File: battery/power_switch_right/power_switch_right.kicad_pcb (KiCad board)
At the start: 2 copper layers, 1 part

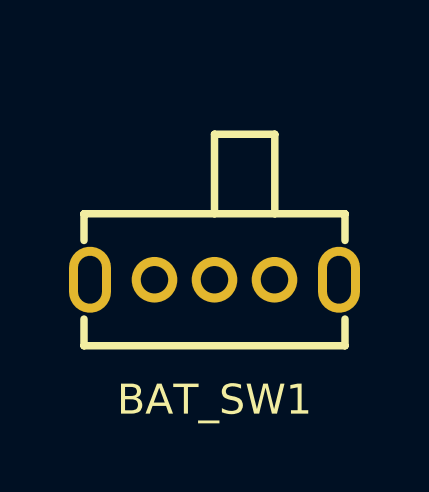
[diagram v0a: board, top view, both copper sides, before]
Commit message: use SK12D07VG5
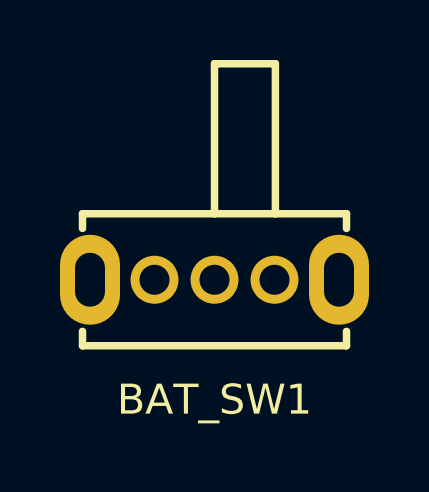
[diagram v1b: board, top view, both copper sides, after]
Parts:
- BAT_SW1: value ~ -> SK12D07VG5; footprint ErgoCai.pretty:SW-TH_SK12D07VG4 -> ErgoCai.pretty:SW-TH_SK12D07VG5-1
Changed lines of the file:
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@@
 	(net 3 "GND")
 	(net 4 "unconnected-(BAT_SW1-Pad3)")
-	(footprint "ErgoCai.pretty:SW-TH_SK12D07VG4"
+	(footprint "ErgoCai.pretty:SW-TH_SK12D07VG5-1"
 		(layer "F.Cu")
 		(at 0 0 180)
 		(property "Reference" "BAT_SW1"
-			(at 0 -4 180)
-			(layer "F.SilkS")
-			(effects
-				(font
-					(size 1 1)
-					(thickness 0.15)
-				)
-			)
-		)
-		(property "Value" "~"
-			(at 0 4 180)
-			(layer "F.Fab")
-			(effects
-				(font
-					(size 1 1)
-					(thickness 0.15)
-				)
-			)
-		)
-		(property "Datasheet" "https://lcsc.com/product-detail/Toggle-Switches_SHOU-HAN-SK12D07VG4_C393937.html"
-			(at 0 0 180)
+			(at 0 -4 0)
+			(layer "F.SilkS")
+			(effects
+				(font
+					(size 1 1)
+					(thickness 0.15)
+				)
+			)
+		)
+		(property "Value" "SK12D07VG5"
+			(at 0 4 0)
+			(layer "F.Fab")
+			(effects
+				(font
+					(size 1 1)
+					(thickness 0.15)
+				)
+			)
+		)
+		(property "Datasheet" "https://lcsc.com/product-detail/Toggle-Switches_SHOU-HAN-SK12D07VG5_C431548.html"
+			(at 0 0 0)
 			(layer "F.Fab")
 			(hide yes)
@@
 			)
 		)
-		(property "Description" "Switch, dual pole double throw, separate symbols"
-			(at 0 0 180)
+		(property "Description" ""
+			(at 0 0 0)
 			(layer "F.Fab")
 			(hide yes)
@@
 			)
 		)
-		(property "MF" "C&K"
-			(at 0 0 180)
-			(unlocked yes)
-			(layer "F.Fab")
-			(hide yes)
-			(effects
-				(font
-					(size 1 1)
-					(thickness 0.15)
-				)
-			)
-		)
-		(property "Description_1" "Switch Slide ON ON SPDT Side Slide 0.3A 30VDC PC Pins Bracket Mount/Through Hole Bulk"
-			(at 0 0 180)
-			(unlocked yes)
-			(layer "F.Fab")
-			(hide yes)
-			(effects
-				(font
-					(size 1 1)
-					(thickness 0.15)
-				)
-			)
-		)
-		(property "Package" "None"
-			(at 0 0 180)
-			(unlocked yes)
-			(layer "F.Fab")
-			(hide yes)
-			(effects
-				(font
-					(size 1 1)
-					(thickness 0.15)
-				)
-			)
-		)
-		(property "Price" "None"
-			(at 0 0 180)
-			(unlocked yes)
-			(layer "F.Fab")
-			(hide yes)
-			(effects
-				(font
-					(size 1 1)
-					(thickness 0.15)
-				)
-			)
-		)
-		(property "SnapEDA_Link" "https://www.snapeda.com/parts/SK12D07VG4/C%2526K/view-part/?ref=snap"
-			(at 0 0 180)
-			(unlocked yes)
-			(layer "F.Fab")
-			(hide yes)
-			(effects
-				(font
-					(size 1 1)
-					(thickness 0.15)
-				)
-			)
-		)
-		(property "MP" "SK12D07VG4"
-			(at 0 0 180)
-			(unlocked yes)
-			(layer "F.Fab")
-			(hide yes)
-			(effects
-				(font
-					(size 1 1)
-					(thickness 0.15)
-				)
-			)
-		)
-		(property "Availability" "Not in stock"
-			(at 0 0 180)
-			(unlocked yes)
-			(layer "F.Fab")
-			(hide yes)
-			(effects
-				(font
-					(size 1 1)
-					(thickness 0.15)
-				)
-			)
-		)
-		(property "Check_prices" "https://www.snapeda.com/parts/SK12D07VG4/C%2526K/view-part/?ref=eda"
-			(at 0 0 180)
-			(unlocked yes)
-			(layer "F.Fab")
-			(hide yes)
-			(effects
-				(font
-					(size 1 1)
-					(thickness 0.15)
-				)
-			)
-		)
-		(property "LCSC Part" "C393937"
+		(property "LCSC Part" "C431548"
 			(at 0 0 180)
 			(unlocked yes)
@@
 		(attr through_hole)
 		(fp_line
-			(start 4.35 2.2)
-			(end -4.35 2.2)
-			(stroke
-				(width 0.25)
-				(type solid)
-			)
-			(layer "F.SilkS")
-		)
-		(fp_line
-			(start 4.35 1.31)
-			(end 4.35 2.2)
-			(stroke
-				(width 0.25)
-				(type solid)
-			)
-			(layer "F.SilkS")
-		)
-		(fp_line
-			(start 4.35 -2.2)
-			(end 4.35 -1.31)
-			(stroke
-				(width 0.25)
-				(type solid)
-			)
-			(layer "F.SilkS")
-		)
-		(fp_line
-			(start 0 4.85)
-			(end 0 2.2)
-			(stroke
-				(width 0.25)
-				(type solid)
-			)
-			(layer "F.SilkS")
-		)
-		(fp_line
-			(start -2.01 4.85)
-			(end 0 4.85)
-			(stroke
-				(width 0.25)
-				(type solid)
-			)
-			(layer "F.SilkS")
-		)
-		(fp_line
-			(start -2.01 2.2)
-			(end -2.01 4.85)
-			(stroke
-				(width 0.25)
-				(type solid)
-			)
-			(layer "F.SilkS")
-		)
-		(fp_line
-			(start -4.35 2.2)
-			(end -4.35 1.31)
-			(stroke
-				(width 0.25)
-				(type solid)
-			)
-			(layer "F.SilkS")
-		)
-		(fp_line
-			(start -4.35 -1.31)
-			(end -4.35 -2.2)
-			(stroke
-				(width 0.25)
-				(type solid)
-			)
-			(layer "F.SilkS")
-		)
-		(fp_line
-			(start -4.35 -2.2)
-			(end 4.35 -2.2)
+			(start 4.4 2.2)
+			(end -4.4 2.2)
+			(stroke
+				(width 0.25)
+				(type solid)
+			)
+			(layer "F.SilkS")
+		)
+		(fp_line
+			(start 4.4 1.71)
+			(end 4.4 2.2)
+			(stroke
+				(width 0.25)
+				(type solid)
+			)
+			(layer "F.SilkS")
+		)
+		(fp_line
+			(start 4.4 -2.2)
+			(end 4.4 -1.72)
+			(stroke
+				(width 0.25)
+				(type solid)
+			)
+			(layer "F.SilkS")
+		)
+		(fp_line
+			(start 4.4 -2.2)
+			(end -4.4 -2.2)
+			(stroke
+				(width 0.25)
+				(type solid)
+			)
+			(layer "F.SilkS")
+		)
+		(fp_line
+			(start 0 2.2)
+			(end 0 7.2)
+			(stroke
+				(width 0.25)
+				(type solid)
+			)
+			(layer "F.SilkS")
+		)
+		(fp_line
+			(start -2.03 7.2)
+			(end 0 7.2)
+			(stroke
+				(width 0.25)
+				(type solid)
+			)
+			(layer "F.SilkS")
+		)
+		(fp_line
+			(start -2.03 7.2)
+			(end -2.03 2.2)
+			(stroke
+				(width 0.25)
+				(type solid)
+			)
+			(layer "F.SilkS")
+		)
+		(fp_line
+			(start -4.4 1.71)
+			(end -4.4 2.2)
+			(stroke
+				(width 0.25)
+				(type solid)
+			)
+			(layer "F.SilkS")
+		)
+		(fp_line
+			(start -4.4 -2.2)
+			(end -4.4 -1.72)
 			(stroke
 				(width 0.25)
@@
 		)
 		(fp_rect
-			(start -4.9 -2.4)
-			(end 4.9 2.4)
+			(start -5.5 -2.5)
+			(end 5.5 2.5)
 			(stroke
 				(width 0.05)
-				(type solid)
+				(type default)
 			)
 			(fill no)
 			(layer "F.CrtYd")
 		)
-		(fp_circle
-			(center -4.47 2.2)
-			(end -4.44 2.2)
-			(stroke
-				(width 0.06)
-				(type solid)
-			)
-			(fill no)
-			(layer "F.Fab")
-		)
 		(fp_text user "${REFERENCE}"
-			(at 0 0 180)
-			(layer "F.Fab")
-			(effects
-				(font
-					(size 1 1)
-					(thickness 0.15)
-				)
-			)
-		)
-		(pad "1" thru_hole circle
-			(at -2 0 180)
-			(size 1.52 1.52)
-			(drill 0.9144)
+			(at 0 0 0)
+			(layer "F.Fab")
+			(effects
+				(font
+					(size 1 1)
+					(thickness 0.15)
+				)
+			)
+		)
+		(pad "1" thru_hole oval
+			(at -2 0)
+			(size 1.6 1.6)
+			(drill 0.999998)
 			(layers "*.Cu" "*.Mask")
 			(remove_unused_layers no)
@@
 			(pintype "unspecified")
 		)
-		(pad "2" thru_hole circle
-			(at 0 0 180)
-			(size 1.52 1.52)
-			(drill 0.9144)
+		(pad "2" thru_hole oval
+			(at 0 0)
+			(size 1.6 1.6)
+			(drill 0.999998)
 			(layers "*.Cu" "*.Mask")
 			(remove_unused_layers no)
@@
 			(pintype "unspecified")
 		)
-		(pad "3" thru_hole circle
-			(at 2 0 180)
-			(size 1.52 1.52)
-			(drill 0.9144)
+		(pad "3" thru_hole oval
+			(at 2 0)
+			(size 1.6 1.6)
+			(drill 0.999998)
 			(layers "*.Cu" "*.Mask")
 			(remove_unused_layers no)
@@
 		)
 		(pad "4" thru_hole oval
-			(at 4.15 0 180)
-			(size 1.4 2.2)
-			(drill oval 0.799998 1.599997)
+			(at 4.15 0 90)
+			(size 3 2)
+			(drill oval 1.799996 0.999998)
 			(layers "*.Cu" "*.Mask")
 			(remove_unused_layers no)
@@
 		)
 		(pad "5" thru_hole oval
-			(at -4.15 0 180)
-			(size 1.4 2.2)
-			(drill oval 0.799998 1.599997)
+			(at -4.15 0 90)
+			(size 3 2)
+			(drill oval 1.799996 0.999998)
 			(layers "*.Cu" "*.Mask")
 			(remove_unused_layers no)
@@
 		)
 		(embedded_fonts no)
-		(model "/Users/jinsongc/Development/ErgoCaiLib/3dmodels/SW-TH_L8.7-W4.4-H4.0-P2.0.step"
+		(model "/Users/jinsongc/Development/ErgoCaiLib/3dmodels/SW-TH_SK12D07VG5-1.step"
 			(offset
-				(xyz 0 -0 0)
+				(xyz 0 -2 4.5)
 			)
 			(scale

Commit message: update power switch
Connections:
- BAT_SW1 pad 1: VSYS -> unconnected-(BAT_SW1-Pad1)
- BAT_SW1 pad 3: unconnected-(BAT_SW1-Pad3) -> VSYS
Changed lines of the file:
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@@
 	(net 2 "VSYS")
 	(net 3 "GND")
-	(net 4 "unconnected-(BAT_SW1-Pad3)")
+	(net 4 "unconnected-(BAT_SW1-Pad1)")
 	(footprint "ErgoCai.pretty:SW-TH_SK12D07VG5-1"
 		(layer "F.Cu")
@@
 			(layers "*.Cu" "*.Mask")
 			(remove_unused_layers no)
-			(net 2 "VSYS")
+			(net 4 "unconnected-(BAT_SW1-Pad1)")
 			(pinfunction "1")
-			(pintype "unspecified")
+			(pintype "unspecified+no_connect")
 		)
 		(pad "2" thru_hole oval
@@
 			(layers "*.Cu" "*.Mask")
 			(remove_unused_layers no)
-			(net 4 "unconnected-(BAT_SW1-Pad3)")
+			(net 2 "VSYS")
 			(pinfunction "3")
-			(pintype "unspecified+no_connect")
+			(pintype "unspecified")
 		)
 		(pad "4" thru_hole oval
